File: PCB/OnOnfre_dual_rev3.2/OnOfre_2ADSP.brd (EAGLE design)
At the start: 44.4 x 47.7 mm, 24 parts, among them J3Y S8050, J6 8p, J7 8p, K1 OMRON-G3MB-202P-SSR2, K2 OMRON-G3MB-202P-SSR2, U2 esp12

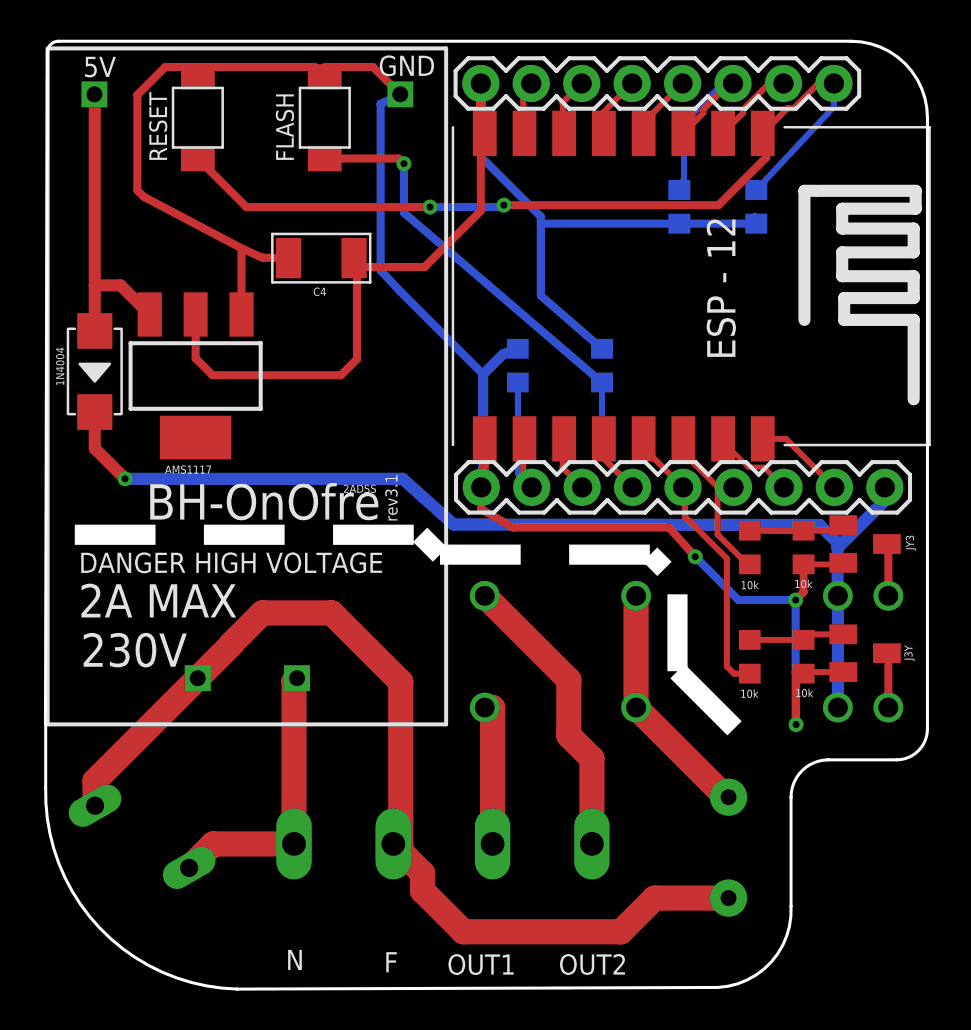
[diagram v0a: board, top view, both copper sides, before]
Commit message: 3.2 Via por baixo do ESP8266 mudada de sitio
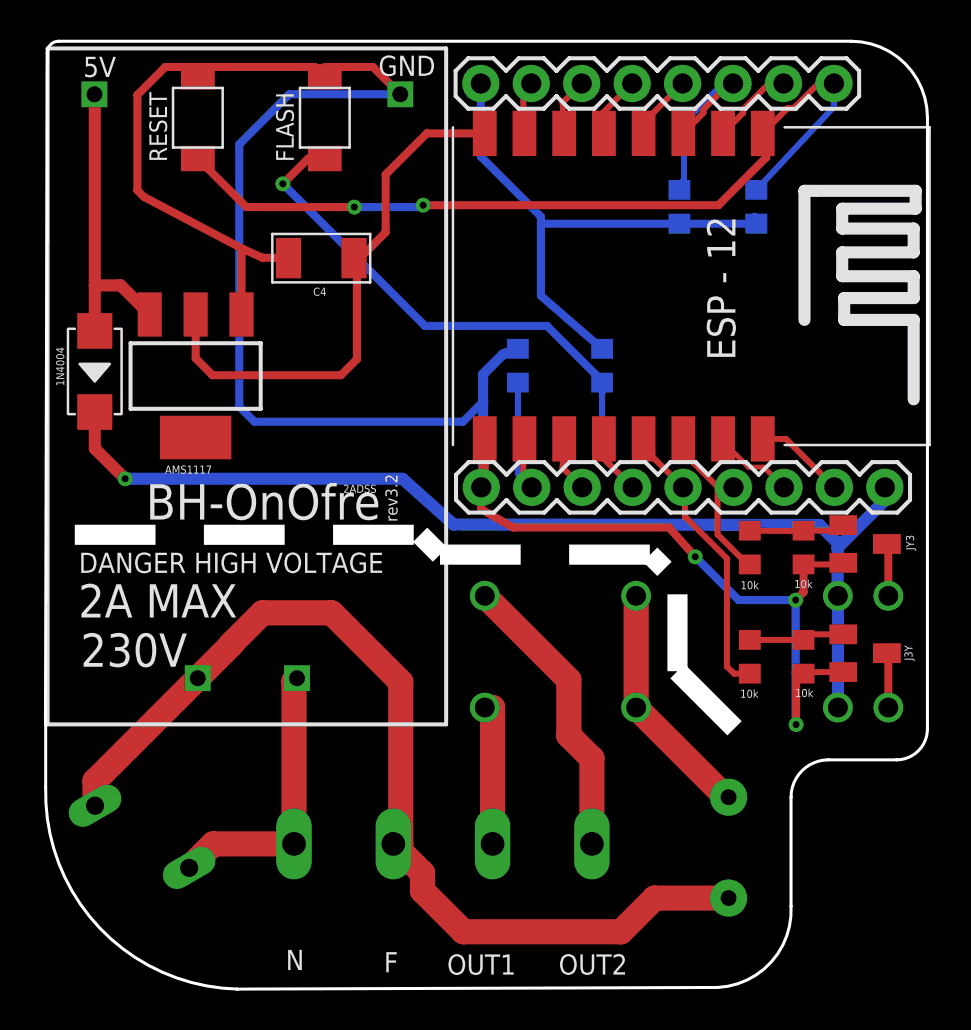
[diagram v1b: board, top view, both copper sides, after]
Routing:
- net GND: track 95.4 -> 113.9 mm
- net 3V3: track 60.2 -> 54.2 mm
- net GPIO0: track 28.7 -> 32.3 mm
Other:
- board text added: "rev3.2"
- board text removed: "rev3.1"
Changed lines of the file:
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@@
 <wire x1="32.2216125" y1="18.487096875" x2="32.2216125" y2="14.613959375" width="1.016" layer="46" style="shortdash"/>
 <wire x1="32.2216125" y1="14.613959375" x2="36.81131875" y2="10.024253125" width="1.016" layer="46" style="shortdash"/>
-<text x="18.12618125" y="22.133634375" size="0.6096" layer="25" rot="R90">rev3.1</text>
+<text x="18.12618125" y="22.133634375" size="0.6096" layer="25" rot="R90">rev3.2</text>
 <text x="15.387978125" y="23.598921875" size="0.4064" layer="25">2ADSS</text>
 <wire x1="0.508" y1="11.938" x2="20.574" y2="11.938" width="0.2" layer="25"/>
@@
 <wire x1="24.186890625" y1="30.85" x2="23.438009375" y2="30.571334375" width="0.508" layer="16"/>
 <wire x1="23.438009375" y1="30.571334375" x2="22.436378125" y2="29.569703125" width="0.508" layer="16"/>
-<wire x1="22.436378125" y1="29.569703125" x2="22.436378125" y2="23.967046875" width="0.508" layer="16"/>
+<wire x1="22.436378125" y1="29.569703125" x2="22.436378125" y2="29.21" width="0.508" layer="16"/>
+<wire x1="22.436378125" y1="29.21" x2="22.436378125" y2="28.194" width="0.508" layer="16"/>
+<wire x1="22.436378125" y1="28.194" x2="22.436378125" y2="23.967046875" width="0.508" layer="16"/>
 <wire x1="22.436378125" y1="23.967046875" x2="22.342321875" y2="23.872990625" width="0.508" layer="16"/>
 <wire x1="38.57136875" y1="19.992975" x2="40.698790625" y2="19.992975" width="0.3048" layer="1"/>
@@
 <wire x1="33.116590625" y1="20.37745" x2="35.295878125" y2="18.1981625" width="0.4064" layer="16"/>
 <wire x1="35.295878125" y1="18.1981625" x2="38.1717" y2="18.1981625" width="0.4064" layer="16"/>
-<wire x1="22.436378125" y1="29.569703125" x2="18.264703125" y2="33.741378125" width="0.4064" layer="16"/>
 <wire x1="5.353690625" y1="38.499878125" x2="10.3417375" y2="35.874340625" width="0.4064" layer="1"/>
 <wire x1="10.3417375" y1="35.874340625" x2="11.319228125" y2="35.43694375" width="0.4064" layer="1"/>
@@
 <wire x1="14.46374375" y1="44.5410625" x2="13.9632125" y2="45.04159375" width="0.4064" layer="1"/>
 <wire x1="13.9632125" y1="45.04159375" x2="8.128" y2="45.04159375" width="0.4064" layer="1"/>
-<wire x1="18.264703125" y1="33.741378125" x2="17.272" y2="34.798" width="0.4064" layer="16"/>
-<wire x1="17.272" y1="34.798" x2="17.272" y2="43.18" width="0.4064" layer="16"/>
-<wire x1="17.272" y1="43.18" x2="18.264703125" y2="43.66316875" width="0.4064" layer="16"/>
+<wire x1="18.264703125" y1="43.66316875" x2="12.67516875" y2="43.66316875" width="0.4064" layer="16"/>
+<wire x1="12.67516875" y1="43.66316875" x2="10.16" y2="41.148" width="0.4064" layer="16"/>
+<wire x1="10.16" y1="41.148" x2="10.16" y2="27.94" width="0.4064" layer="16"/>
+<wire x1="10.16" y1="27.94" x2="10.922" y2="27.178" width="0.4064" layer="16"/>
+<wire x1="10.922" y1="27.178" x2="21.420378125" y2="27.178" width="0.4064" layer="16"/>
+<wire x1="21.420378125" y1="27.178" x2="22.436378125" y2="28.194" width="0.4064" layer="16"/>
 </signal>
 <signal name="VCC">
@@
 <wire x1="29.962321875" y1="23.872990625" x2="28.434640625" y2="25.400671875" width="0.3048" layer="1"/>
 <wire x1="28.434640625" y1="25.400671875" x2="28.516375" y2="26.31254375" width="0.3048" layer="1"/>
-<wire x1="28.424503125" y1="29.15" x2="28.424503125" y2="25.410809375" width="0.3048" layer="16"/>
+<wire x1="28.424503125" y1="29.15" x2="28.424503125" y2="28.702" width="0.3048" layer="16"/>
+<wire x1="28.424503125" y1="28.702" x2="28.424503125" y2="25.410809375" width="0.3048" layer="16"/>
 <wire x1="28.424503125" y1="25.410809375" x2="29.962321875" y2="23.872990625" width="0.3048" layer="16"/>
-<wire x1="28.424503125" y1="29.15" x2="18.44741875" y2="37.70026875" width="0.4064" layer="16"/>
-<wire x1="18.44741875" y1="37.70026875" x2="18.44741875" y2="40.1707625" width="0.4064" layer="16"/>
-<via x="18.44741875" y="40.1707625" extent="1-16" drill="0.35"/>
-<wire x1="14.46374375" y1="40.4298625" x2="18.18831875" y2="40.4298625" width="0.4064" layer="1"/>
-<wire x1="18.18831875" y1="40.4298625" x2="18.44741875" y2="40.1707625" width="0.4064" layer="1"/>
+<via x="12.35141875" y="39.1547625" extent="1-16" drill="0.35"/>
+<wire x1="14.46374375" y1="40.4298625" x2="13.62651875" y2="40.4298625" width="0.4064" layer="1"/>
+<wire x1="13.62651875" y1="40.4298625" x2="12.35141875" y2="39.1547625" width="0.4064" layer="1"/>
+<wire x1="12.35141875" y1="39.1547625" x2="15.974090625" y2="35.532090625" width="0.4064" layer="16"/>
+<wire x1="15.974090625" y1="35.532090625" x2="16.228090625" y2="35.278090625" width="0.4064" layer="16"/>
+<wire x1="16.228090625" y1="35.278090625" x2="19.50218125" y2="32.004" width="0.4064" layer="16"/>
+<wire x1="19.50218125" y1="32.004" x2="25.654" y2="32.004" width="0.4064" layer="16"/>
+<wire x1="25.654" y1="32.004" x2="28.424503125" y2="29.233496875" width="0.4064" layer="16"/>
+<wire x1="28.424503125" y1="29.233496875" x2="28.424503125" y2="28.702" width="0.4064" layer="16"/>
 </signal>
 <signal name="RESET">
@@
 <wire x1="36.19259375" y1="38.85" x2="40.100071875" y2="43.031684375" width="0.3048" layer="16"/>
 <wire x1="40.100071875" y1="43.031684375" x2="40.100071875" y2="44.209115625" width="0.3048" layer="16"/>
-<via x="19.76265625" y="37.986565625" extent="1-16" drill="0.35"/>
-<wire x1="19.76265625" y1="37.986565625" x2="23.38306875" y2="37.986234375" width="0.4064" layer="16"/>
-<wire x1="23.38306875" y1="37.986234375" x2="23.478178125" y2="38.08134375" width="0.4064" layer="16"/>
-<via x="23.478178125" y="38.08134375" extent="1-16" drill="0.35"/>
-<wire x1="23.478178125" y1="38.08134375" x2="34.284915625" y2="38.08134375" width="0.4064" layer="1"/>
-<wire x1="34.284915625" y1="38.08134375" x2="36.692840625" y2="40.48926875" width="0.4064" layer="1"/>
+<via x="15.95265625" y="37.986565625" extent="1-16" drill="0.35"/>
+<via x="19.414178125" y="38.08134375" extent="1-16" drill="0.35"/>
+<wire x1="36.692840625" y1="40.48926875" x2="34.284915625" y2="38.08134375" width="0.4064" layer="1"/>
 <wire x1="36.692840625" y1="40.48926875" x2="36.692840625" y2="41.875896875" width="0.4064" layer="1"/>
 <wire x1="8.0712" y1="40.4298625" x2="10.514496875" y2="37.986565625" width="0.4064" layer="1"/>
-<wire x1="10.514496875" y1="37.986565625" x2="19.76265625" y2="37.986565625" width="0.4064" layer="1"/>
+<wire x1="10.514496875" y1="37.986565625" x2="15.95265625" y2="37.986565625" width="0.4064" layer="1"/>
+<wire x1="34.284915625" y1="38.08134375" x2="19.414178125" y2="38.08134375" width="0.4064" layer="1"/>
+<wire x1="15.95265625" y1="37.986565625" x2="19.3194" y2="37.986565625" width="0.4064" layer="16"/>
+<wire x1="19.3194" y1="37.986565625" x2="19.414178125" y2="38.08134375" width="0.4064" layer="16"/>
 </signal>
 <signal name="CH_PD">
@@
 <contactref element="AMS1117" pad="2"/>
 <contactref element="J7" pad="1"/>
-<wire x1="22.320071875" y1="44.209115625" x2="22.320071875" y2="41.74980625" width="0.508" layer="1"/>
-<wire x1="22.320071875" y1="41.74980625" x2="22.516375" y2="41.69654375" width="0.508" layer="1"/>
-<wire x1="22.320071875" y1="37.800228125" x2="22.320071875" y2="44.209115625" width="0.4064" layer="1"/>
-<wire x1="19.48849375" y1="34.96865" x2="22.320071875" y2="37.800228125" width="0.4064" layer="1"/>
 <wire x1="28.424503125" y1="30.85" x2="25.342953125" y2="33.520734375" width="0.4064" layer="16"/>
 <wire x1="25.342953125" y1="33.520734375" x2="25.342953125" y2="37.118759375" width="0.4064" layer="16"/>
@@
 <wire x1="16.082175" y1="30.3277" x2="16.082175" y2="35.268109375" width="0.4064" layer="1"/>
 <wire x1="16.082175" y1="35.268109375" x2="15.936078125" y2="35.41420625" width="0.4064" layer="1"/>
-<wire x1="15.936078125" y1="35.41420625" x2="16.381634375" y2="34.96865" width="0.4064" layer="1"/>
-<wire x1="16.381634375" y1="34.96865" x2="19.48849375" y2="34.96865" width="0.4064" layer="1"/>
+<wire x1="16.082175" y1="35.268109375" x2="17.526" y2="36.711934375" width="0.4064" layer="1"/>
+<wire x1="19.59854375" y1="41.69654375" x2="22.516375" y2="41.69654375" width="0.4064" layer="1"/>
+<wire x1="17.526" y1="36.711934375" x2="17.526" y2="39.624" width="0.4064" layer="1"/>
+<wire x1="17.526" y1="39.624" x2="19.59854375" y2="41.69654375" width="0.4064" layer="1"/>
+<wire x1="22.516375" y1="41.69654375" x2="22.320071875" y2="40.52699375" width="0" layer="19" extent="1-16"/>
 </signal>
 <signal name="FASE_IN" class="1">
